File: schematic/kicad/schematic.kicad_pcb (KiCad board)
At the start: 4 copper layers, 80 x 41.2 mm, 19 parts, among them J1 Conn_01x02_Pin, J2 Conn_01x02_Pin, Q1 AO3401, U1 ESP32-C3, U2 MAX4466, U3 HW-373, U4 MT3608, U5 WS2812B

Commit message: Adjust pcb and schematic
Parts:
- added C5: 100nF, Capacitor_THT:C_Disc_D5.0mm_W2.5mm_P5.00mm, F.Cu at (152.4, 93.5)
- added U6: AMS1117, Connector_PinHeader_2.54mm:PinHeader_1x03_P2.54mm_Vertical, F.Cu at (145.5, 84.3)
- C1: value 100uF -> 470uF
- C4: value 470uF -> 100uF
- moved C2 40.6 mm to (188.6, 86.9)
- moved C1 36.8 mm to (182.9, 92.1), turned to -90 degrees
- moved C4 35.0 mm to (182.9, 56.5)
- moved C3 30.4 mm to (188.6, 61.7), turned to -90 degrees
- moved J1 23.0 mm to (160.3, 57.1)
- moved Q1 10.5 mm to (152.4, 57.8)
- moved J2 7.75 mm to (142.9, 57.1)
- moved R1 6.40 mm to (157.0, 65.4)
- moved U4 4.74 mm to (177.2, 74.3)
- moved U3 3.17 mm to (125.7, 63.5)
- moved U1 2.87 mm to (125.1, 83.2)
- moved U2 2.70 mm to (146.7, 90.9), turned to 180 degrees
- moved REF** 2.68 mm to (189.0, 53.8)
- moved REF** 2.67 mm to (113.8, 53.8)
- moved IN5822 2.44 mm to (162.6, 65.4)
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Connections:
- C1 pad 1: Net-(J1-Pin_1) -> +5VA
- C2 pad 1: Net-(J1-Pin_1) -> +5VA
- C3 pad 1: Net-(U1-5V) -> VD
- C4 pad 1: Net-(U1-5V) -> VD
- C6 pad 1: Net-(U1-5V) -> +5VA
- J1 pad 1: Net-(J1-Pin_1) -> Net-(IN5822-K)
- J1 pad 2: Net-(IN5822-K) -> VD
- U1 pad 1: Net-(U1-5V) -> +5VA
- U2 pad 1: Net-(U1-5V) -> Net-(U2-VCC)
- U4 pad 1: Net-(J1-Pin_1) -> VD
- U4 pad 3: Net-(U1-5V) -> +5VA
- U5 pad 3: Net-(U1-5V) -> +5VA
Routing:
- net +5VA: track 0.00 -> 105.4 mm
- net Net-(U1-5V): track 84.3 -> 0.00 mm
- net Net-(J1-Pin_1): track 50.9 -> 0.00 mm
- net VD: track 0.00 -> 35.0 mm
- net Net-(U2-VCC): track 0.00 -> 13.9 mm
- net +5V: track 64.5 -> 73.2 mm
- net Net-(U1-D0): track 27.5 -> 19.0 mm, vias 1 -> 0
- net -BATT: track 11.6 -> 16.3 mm, vias 0 -> 1
- net Net-(IN5822-K): track 24.2 -> 19.5 mm, vias 1 -> 0
- net Net-(Q1-D): track 20.2 -> 22.7 mm
- net GND: track 1.55 -> 0.00 mm
- net Net-(U1-D1): track 39.1 -> 40.1 mm, vias 2 -> 1
- net +BATT: track 8.60 -> 7.92 mm
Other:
- board size 80 x 41.2 mm -> 80 x 45.6 mm

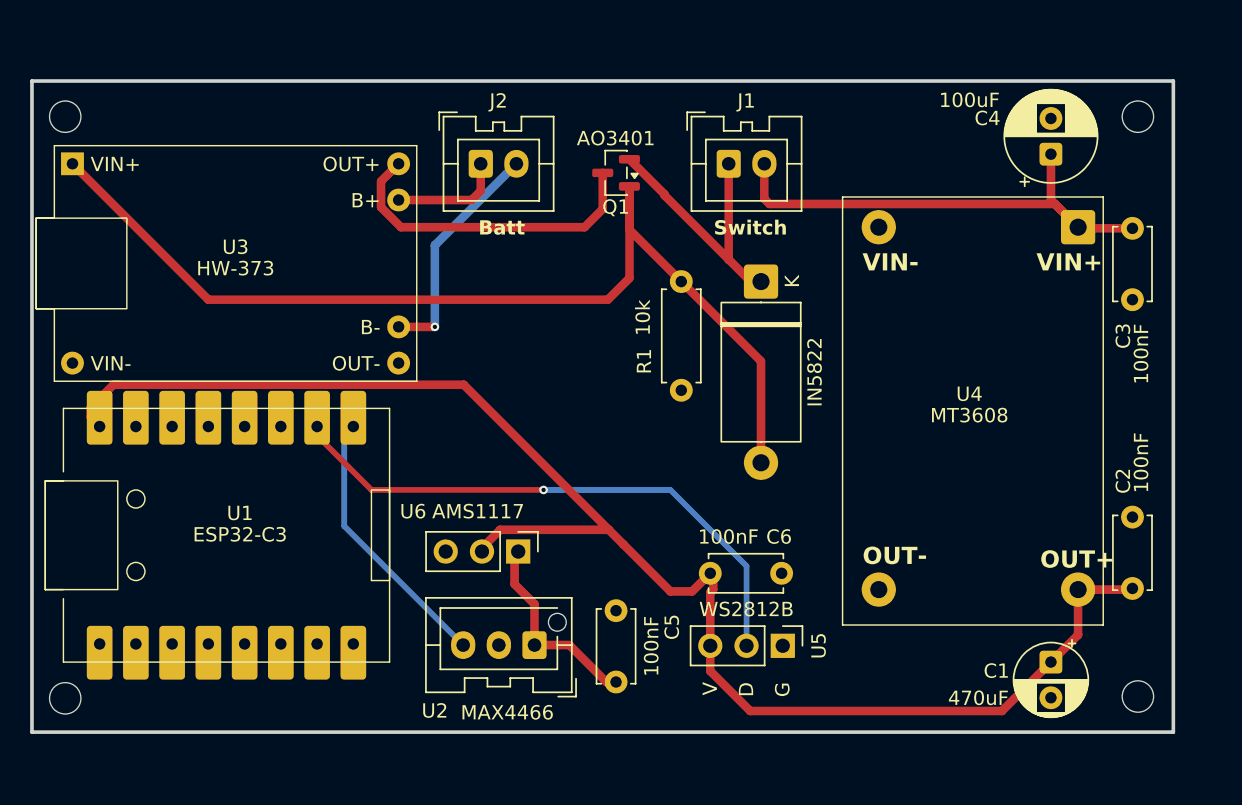
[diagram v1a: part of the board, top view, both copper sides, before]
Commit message: Add extra signal resistor, update schematic and pcb
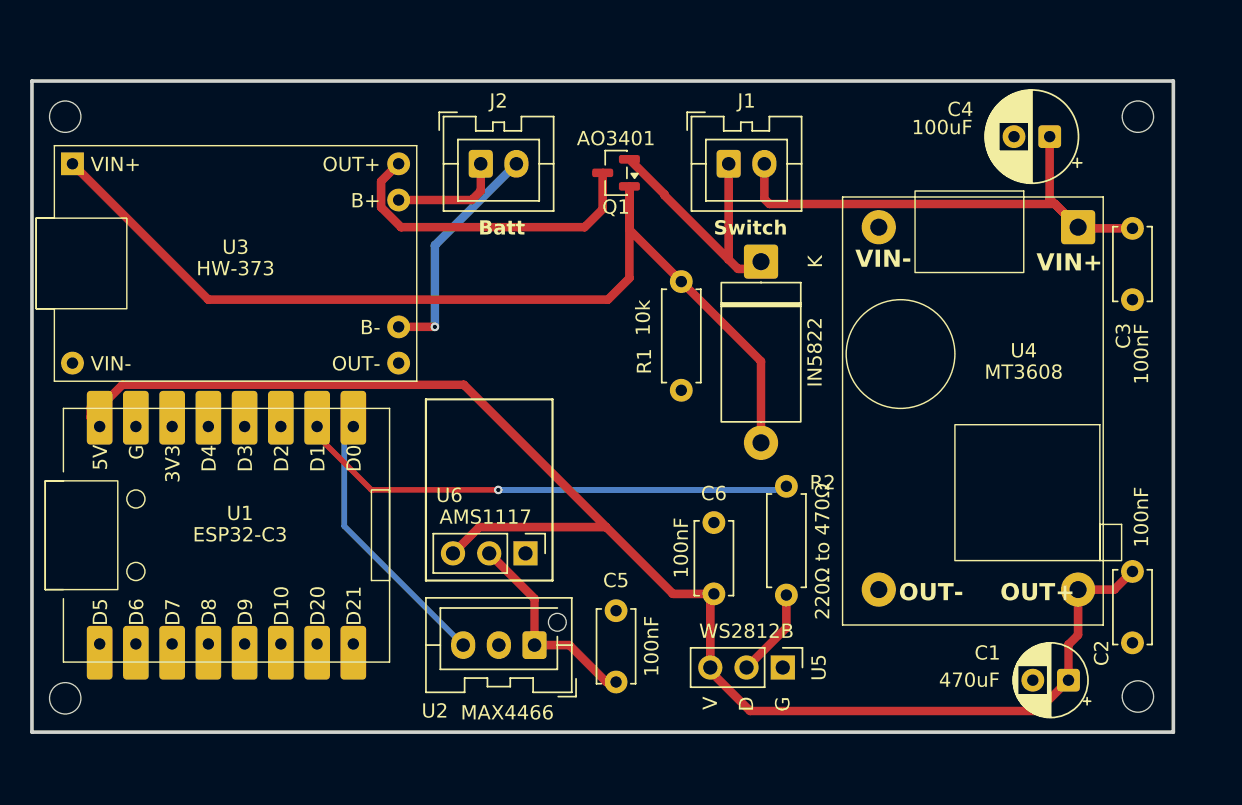
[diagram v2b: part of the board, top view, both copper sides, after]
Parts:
- added R2: 220Ω to 470Ω, Resistor_THT:R_Axial_DIN0207_L6.3mm_D2.5mm_P7.62mm_Horizontal, F.Cu at (164.3, 79.8)
- moved C1 1.77 mm to (184.1, 93.3), turned to 180 degrees
- moved U5 1.52 mm to (164.1, 92.5)
- moved C6 1.47 mm to (159.3, 87.3), turned to 90 degrees
- moved IN5822 1.40 mm to (162.6, 64.0)
- moved C4 1.23 mm to (182.8, 55.2), turned to 180 degrees
- moved C2 1.19 mm to (188.6, 85.7), turned to -90 degrees
- moved U6 0.52 mm to (146.1, 84.5)
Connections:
- U5 pad 2: Net-(U1-D1) -> Net-(U5-DIN)
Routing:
- net Net-(U5-DIN): track 0.00 -> 6.24 mm
- net Net-(U1-D1): track 40.1 -> 35.2 mm
- net +5VA: track 105.4 -> 107.8 mm
- net +5V: track 73.2 -> 71.8 mm
- net VD: track 35.0 -> 36.3 mm
- net Net-(U2-VCC): track 13.9 -> 14.5 mm

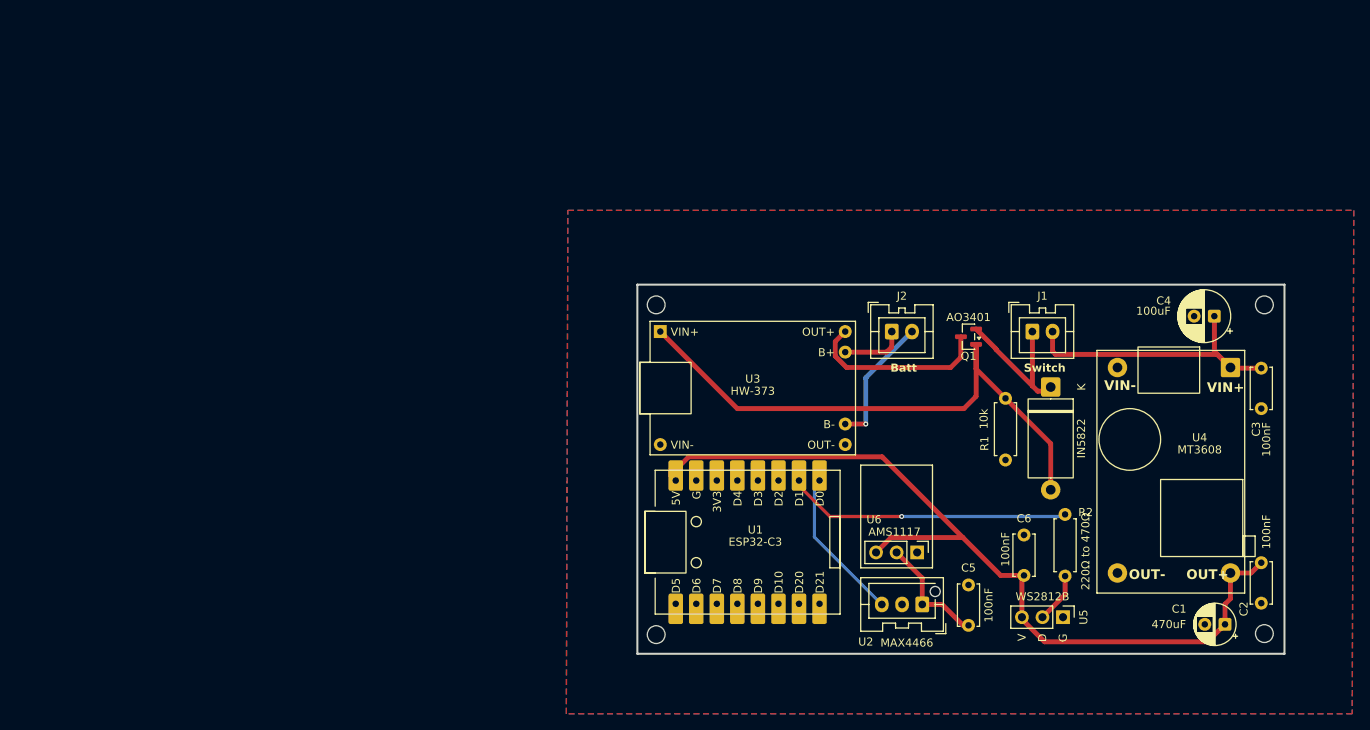
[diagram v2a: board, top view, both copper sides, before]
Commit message: Render + save updated pcb
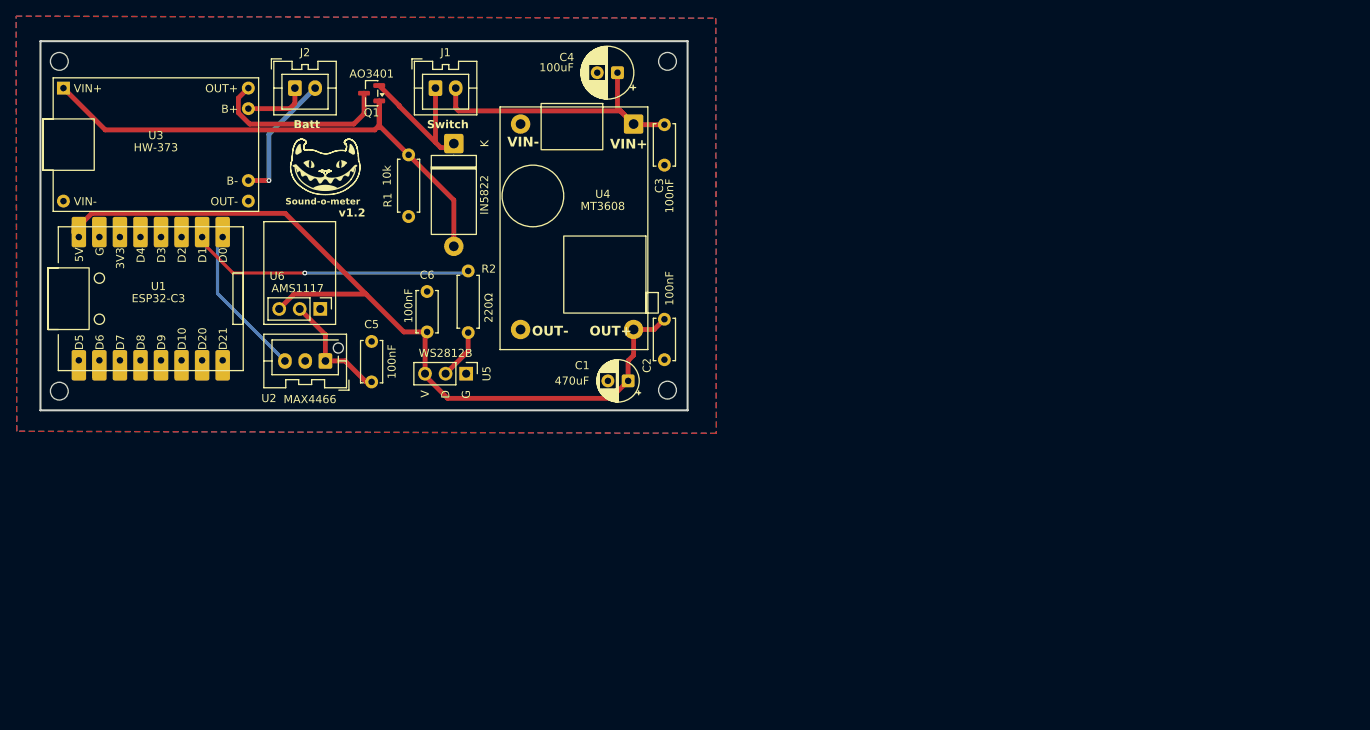
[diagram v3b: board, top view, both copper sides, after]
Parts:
- R2: value 220Ω to 470Ω -> 220Ω
- moved C1 79.7 mm to (110.3, 63.2)
- moved C6 79.7 mm to (85.5, 57.2)
- moved J1 79.7 mm to (86.5, 27.1)
- moved R1 79.7 mm to (83.2, 35.3)
- moved REF** 79.7 mm to (115.2, 64.4)
- moved REF** 79.7 mm to (40.0, 23.7)
- moved REF** 79.7 mm to (115.2, 23.7)
- moved U1 79.7 mm to (51.3, 53.1)
- moved U2 79.7 mm to (72.9, 60.8)
- moved U5 79.7 mm to (90.3, 62.4)
- moved C2 79.7 mm to (114.8, 55.6)
- moved C3 79.7 mm to (114.8, 31.6)
- moved C4 79.7 mm to (109.0, 25.1)
- moved C5 79.7 mm to (78.6, 63.4)
- moved IN5822 79.7 mm to (88.8, 33.9)
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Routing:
- net +5V: track 71.8 -> 66.5 mm
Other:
- board text added: "Sound-o-meter"
- board text added: "v1.2"

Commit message: Fix issues with pcb for JLCPCB
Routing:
- net Net-(U1-D1): track 35.2 -> 36.0 mm
- net +5VA: track 107.8 -> 107.2 mm
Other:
- board text added: "+"
- board text added: "-"
- board text added: "D0"
- board text added: "O"

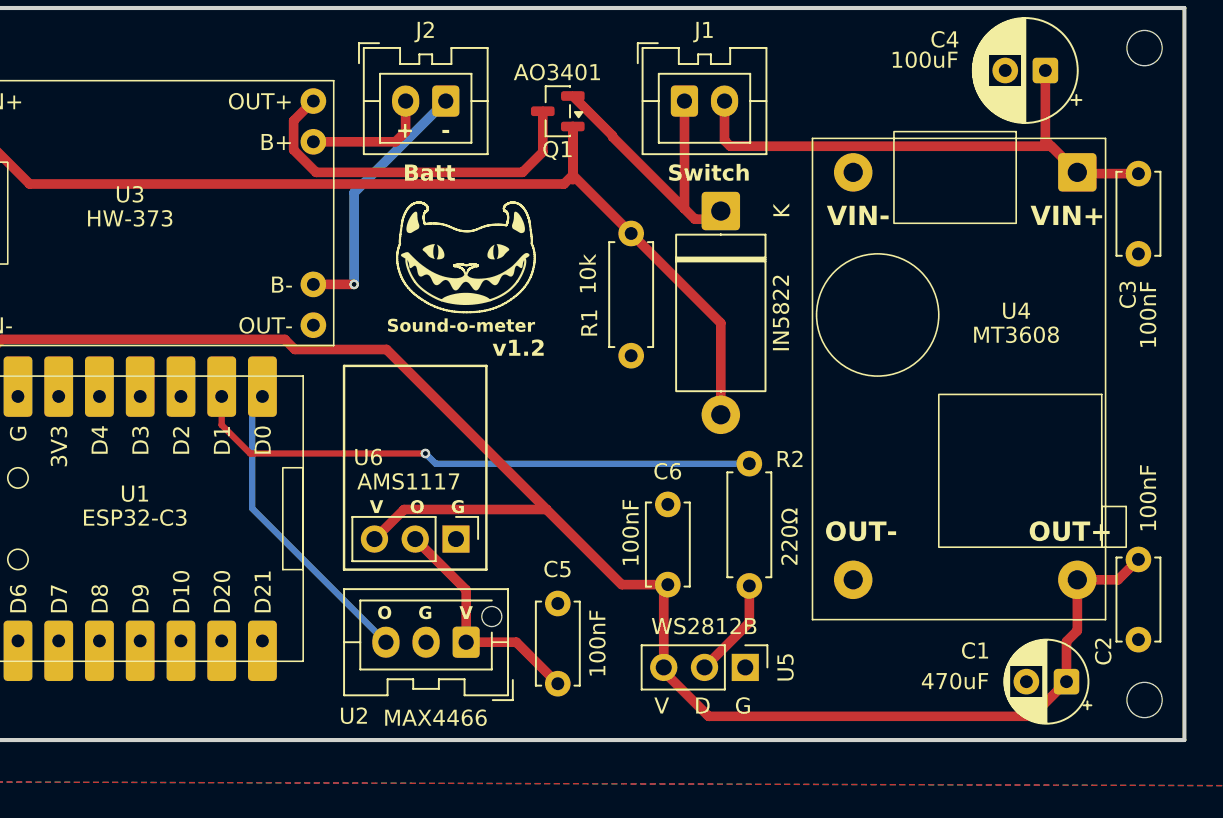
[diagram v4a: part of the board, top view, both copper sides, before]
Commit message: Add battery sense circuit
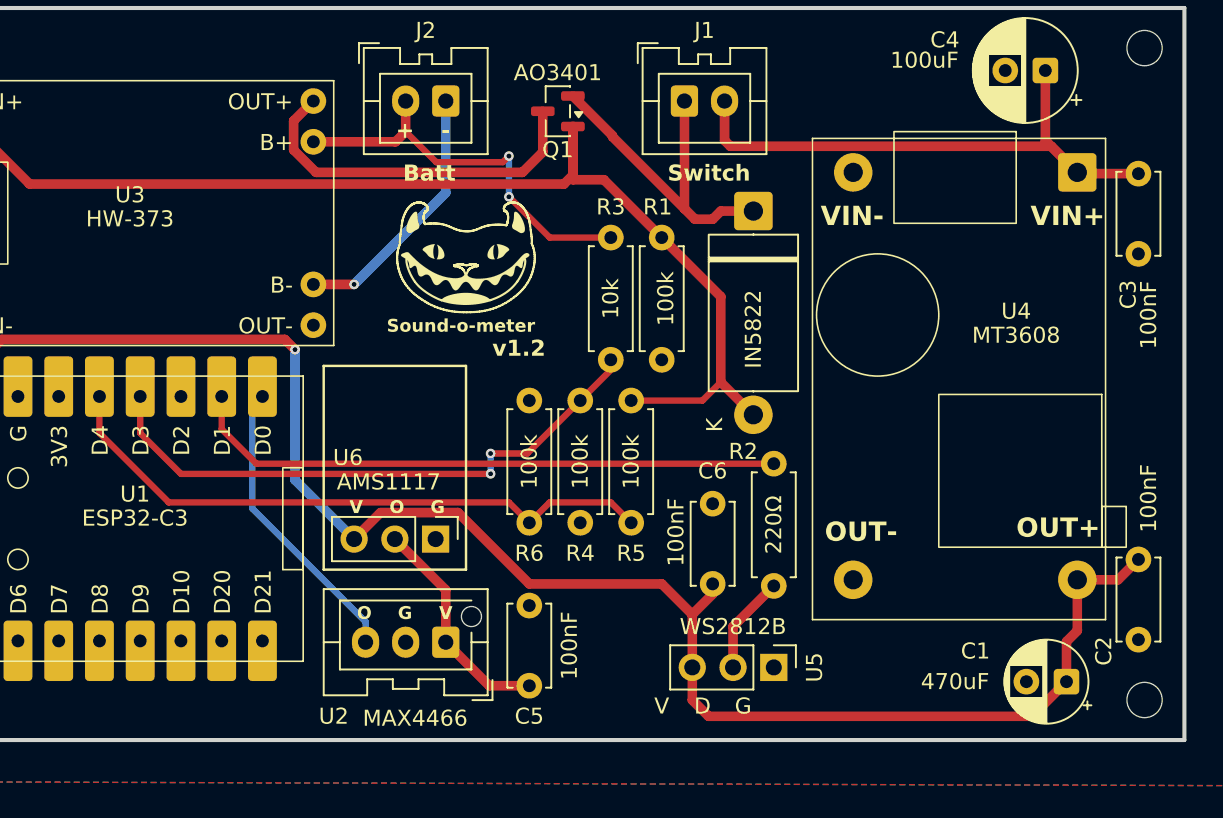
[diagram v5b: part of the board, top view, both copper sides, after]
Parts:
- added R3: 100k, Resistor_THT:R_Axial_DIN0207_L6.3mm_D2.5mm_P7.62mm_Horizontal, F.Cu at (81.9, 43.2)
- added R4: 100k, Resistor_THT:R_Axial_DIN0207_L6.3mm_D2.5mm_P7.62mm_Horizontal, F.Cu at (80.0, 53.3)
- added R5: 100k, Resistor_THT:R_Axial_DIN0207_L6.3mm_D2.5mm_P7.62mm_Horizontal, F.Cu at (83.2, 53.3)
- added R6: 100k, Resistor_THT:R_Axial_DIN0207_L6.3mm_D2.5mm_P7.62mm_Horizontal, F.Cu at (76.8, 45.7)
- moved C6 2.79 mm to (88.3, 57.1)
- moved IN5822 2.03 mm to (90.8, 33.9)
- moved R1 1.92 mm to (85.1, 35.6)
- moved C5 1.78 mm to (76.8, 63.5)
- moved U5 1.78 mm to (92.1, 62.4)
- moved R2 1.52 mm to (92.1, 49.7)
- moved U6 1.27 mm to (71.0, 54.4)
- moved U2 1.27 mm to (71.6, 60.8)
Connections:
- net Net-(U1-D0) renamed MIC
- net Net-(U1-D1) renamed LED
- U1 pad 4: unconnected-(U1-D4-Pad4) -> BATT CHARGE
- U1 pad 5: unconnected-(U1-D3-Pad5) -> BATT LEVEL
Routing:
- net BATT CHARGE: track 0.00 -> 38.8 mm
- net BATT LEVEL: track 0.00 -> 36.7 mm, vias 0 -> 2
- net +BATT: track 7.92 -> 25.2 mm, vias 0 -> 2
- net +5V: track 66.5 -> 74.3 mm
- net +5VA: track 107.2 -> 103.8 mm, vias 0 -> 1
- net Net-(IN5822-K): track 19.4 -> 21.4 mm
- net LED: track 36.0 -> 37.3 mm, vias 1 -> 0
- net MIC: track 19.0 -> 18.5 mm
